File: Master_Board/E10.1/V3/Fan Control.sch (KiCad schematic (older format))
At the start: 12 parts, among them J801 649002227222, J802 649002227222, J803 649002227222, J804 649002227222, Q801 BSS806NH6327XTSA1, Q802 BSS806NH6327XTSA1, Q803 BSS806NH6327XTSA1, Q804 BSS806NH6327XTSA1

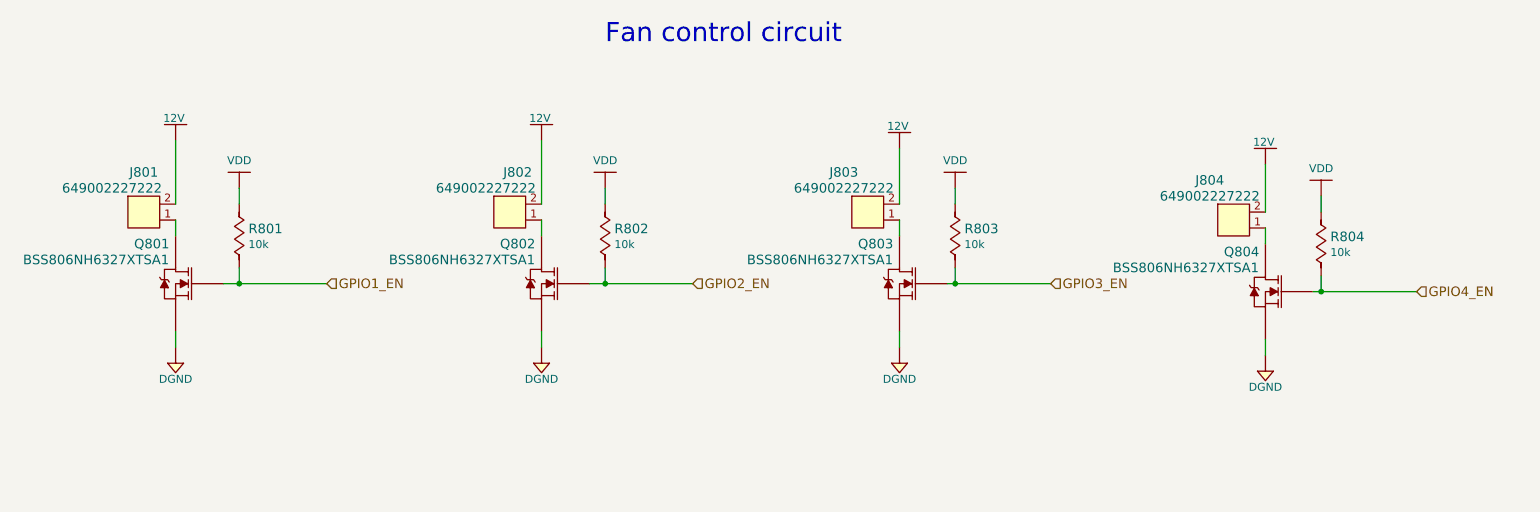
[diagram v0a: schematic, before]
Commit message: 2 new fuses added. PCB traces overhaul to support more current. Some small layout changes.
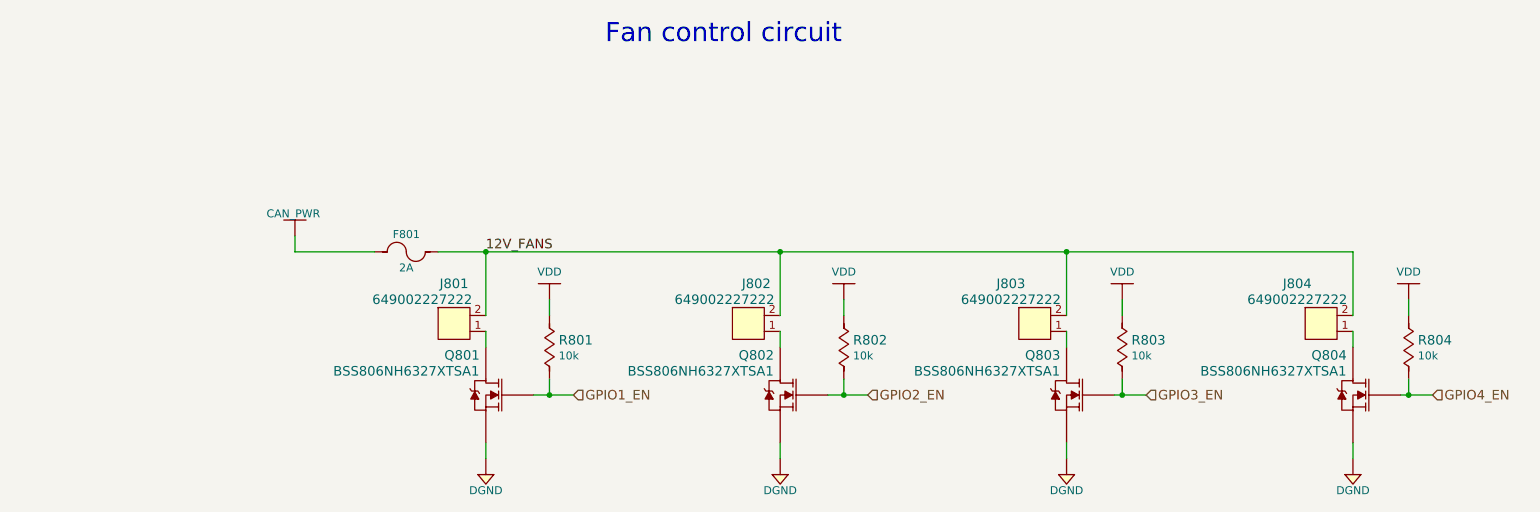
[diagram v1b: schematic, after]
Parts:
- added F801: 39511000440, Fuses:TE5_395, symbol Fuses:39511000440
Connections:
- net 12V renamed 12V_FANS
- net 12V_FANS: now also F801.2
- new net CAN_PWR: F801.1
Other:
- moved on the sheet: J801, J802, J803, J804, Q801, Q802, Q803, Q804, R801, R802, R803, R804
